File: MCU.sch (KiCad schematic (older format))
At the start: 13 parts, among them U5 STM32F405R, Y1 Crystal_8MHz_18pf

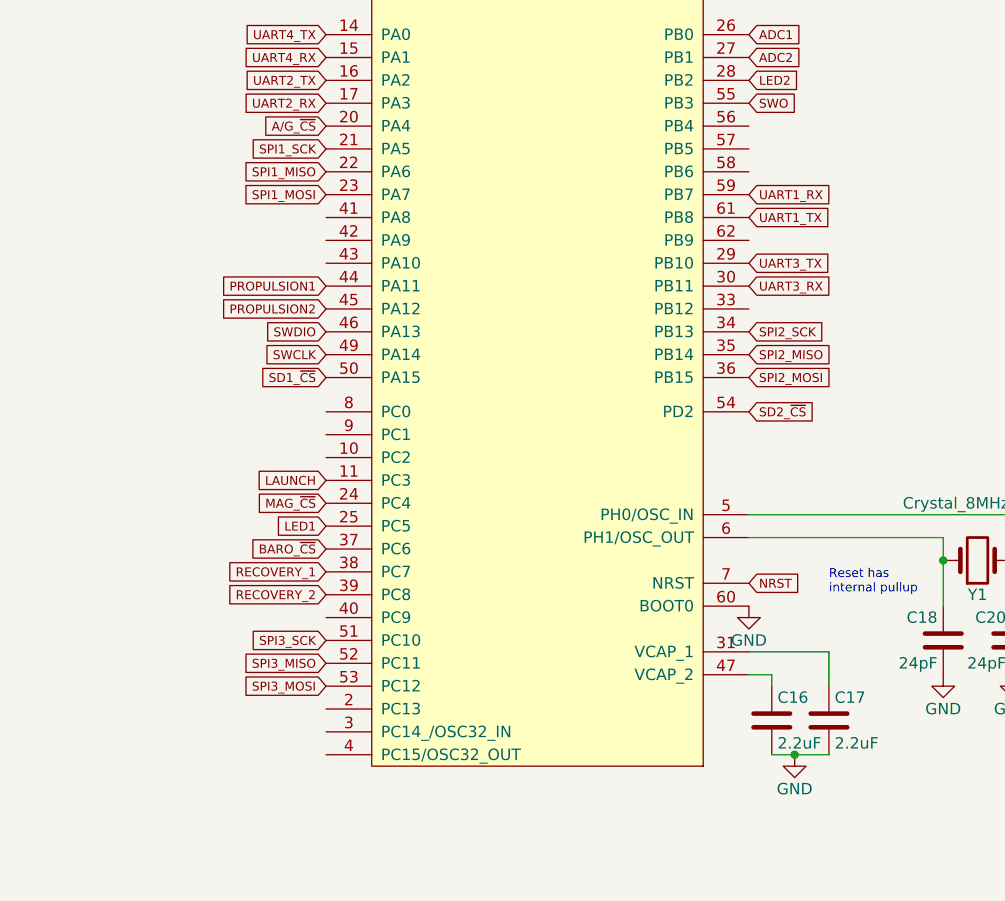
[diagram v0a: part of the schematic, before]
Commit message: Bring schematic in line with PCB. Previous update broke this.
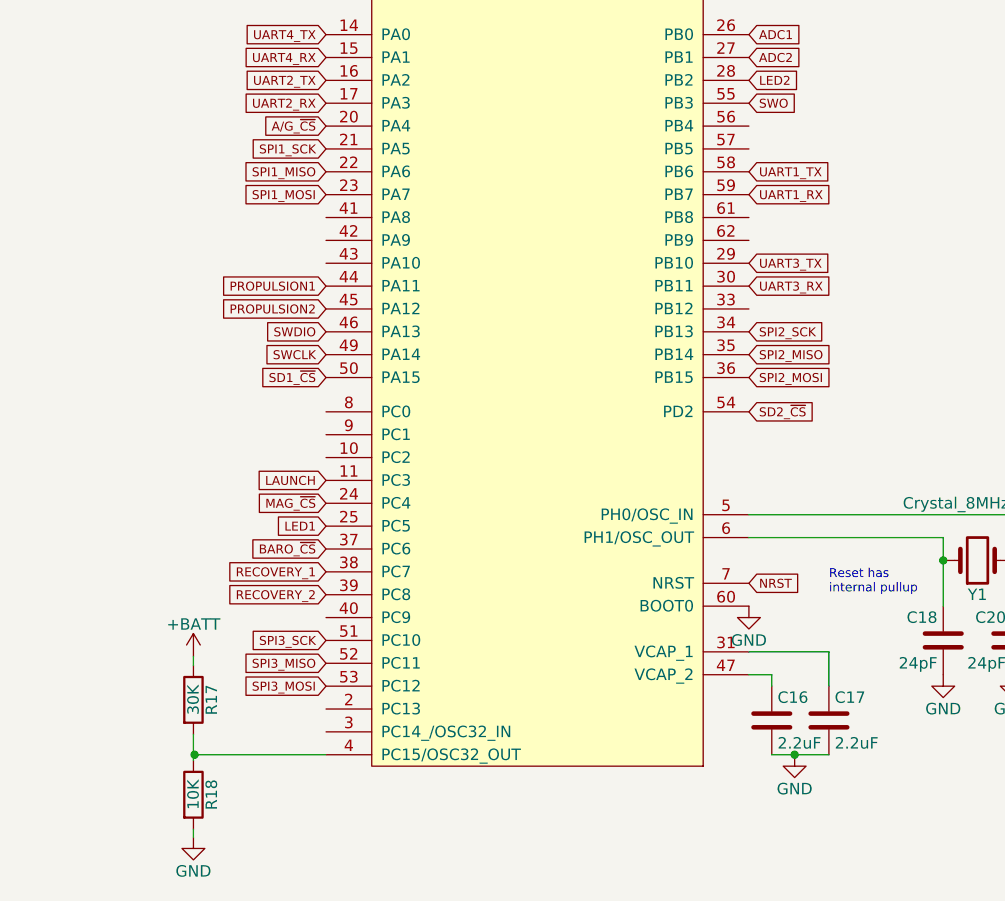
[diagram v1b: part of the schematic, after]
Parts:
- added R17: 30K, Resistors_SMD:R_0603, symbol R
- added R18: 10K, Resistors_SMD:R_0603, symbol R
- C16, C17, C18, C19, C20, C21, C22, C23, C24, C25, C26: footprint Capacitor_SMD:C_0603_1608Metric -> Capacitors_SMD:C_0603
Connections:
- net GND: now also R18.2
- net UART1_TX: now also U5.58 (PB6); no longer U5.61 (PB8)
- net at U5.4 (PC15/OSC32_OUT): now also R17.2, R18.1
- new net +BATT: R17.1
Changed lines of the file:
@@
 EESchema Schematic File Version 2
-LIBS:74xgxx
+LIBS:power
+LIBS:device
+LIBS:switches
+LIBS:relays
+LIBS:motors
+LIBS:transistors
+LIBS:conn
+LIBS:linear
+LIBS:regul
 LIBS:74xx
-LIBS:ac-dc
-LIBS:actel
+LIBS:cmos4000
 LIBS:adc-dac
-LIBS:allegro
-LIBS:Altera
-LIBS:analog_devices
+LIBS:memory
+LIBS:xilinx
+LIBS:microcontrollers
+LIBS:dsp
+LIBS:microchip
 LIBS:analog_switches
+LIBS:motorola
+LIBS:texas
+LIBS:intel
+LIBS:audio
+LIBS:interface
+LIBS:digital-audio
+LIBS:philips
+LIBS:display
+LIBS:cypress
+LIBS:siliconi
+LIBS:opto
 LIBS:atmel
-LIBS:audio
-LIBS:battery_management
-LIBS:bbd
-LIBS:bosch
-LIBS:brooktre
-LIBS:cmos_ieee
-LIBS:cmos4000
-LIBS:conn
 LIBS:contrib
-LIBS:cypress
-LIBS:dc-dc
-LIBS:device
-LIBS:digital-audio
-LIBS:diode
-LIBS:display
-LIBS:dsp
-LIBS:elec-unifil
-LIBS:ESD_Protection
-LIBS:ftdi
-LIBS:gennum
-LIBS:graphic_symbols
-LIBS:hc11
-LIBS:infineon
-LIBS:intel
-LIBS:interface
-LIBS:intersil
-LIBS:ir
-LIBS:Lattice
-LIBS:leds
-LIBS:LEM
-LIBS:linear
-LIBS:logic_programmable
-LIBS:maxim
+LIBS:valves
 LIBS:mechanical
-LIBS:memory
-LIBS:microchip
-LIBS:microchip_dspic33dsc
-LIBS:microchip_pic10mcu
-LIBS:microchip_pic12mcu
-LIBS:microchip_pic16mcu
-LIBS:microchip_pic18mcu
-LIBS:microchip_pic24mcu
-LIBS:microchip_pic32mcu
-LIBS:microcontrollers
-LIBS:modules
-LIBS:motor_drivers
-LIBS:motorola
-LIBS:motors
-LIBS:msp430
-LIBS:nordicsemi
-LIBS:nxp
-LIBS:nxp_armmcu
-LIBS:onsemi
-LIBS:opto
-LIBS:Oscillators
-LIBS:philips
-LIBS:power
-LIBS:Power_Management
-LIBS:powerint
-LIBS:pspice
-LIBS:references
-LIBS:regul
-LIBS:relays
-LIBS:rfcom
-LIBS:RFSolutions
-LIBS:sensors
-LIBS:silabs
-LIBS:siliconi
-LIBS:stm8
-LIBS:stm32
-LIBS:supertex
-LIBS:switches
-LIBS:texas
-LIBS:transf
-LIBS:transistors
-LIBS:triac_thyristor
-LIBS:ttl_ieee
-LIBS:valves
-LIBS:video
-LIBS:wiznet
-LIBS:Worldsemi
-LIBS:Xicor
-LIBS:xilinx
-LIBS:zetex
-LIBS:Zilog
 LIBS:AndromedaV2-cache
 EELAYER 25 0
@@
 F 0 "C19" H 6450 1800 50  0000 L CNN
 F 1 "10uF" H 6450 1600 50  0000 L CNN
-F 2 "Capacitor_SMD:C_0603_1608Metric" H 6463 1550 50  0001 C CNN
+F 2 "Capacitors_SMD:C_0603" H 6463 1550 50  0001 C CNN
 F 3 "" H 6425 1700 50  0001 C CNN
 	1    6425 1700
@@
 F 0 "C21" H 6750 1800 50  0000 L CNN
 F 1 "0.1uF" H 6750 1600 50  0000 L CNN
-F 2 "Capacitor_SMD:C_0603_1608Metric" H 6763 1550 50  0001 C CNN
+F 2 "Capacitors_SMD:C_0603" H 6763 1550 50  0001 C CNN
 F 3 "" H 6725 1700 50  0001 C CNN
 	1    6725 1700
@@
 F 0 "C22" H 7050 1800 50  0000 L CNN
 F 1 "0.1uF" H 7050 1600 50  0000 L CNN
-F 2 "Capacitor_SMD:C_0603_1608Metric" H 7063 1550 50  0001 C CNN
+F 2 "Capacitors_SMD:C_0603" H 7063 1550 50  0001 C CNN
 F 3 "" H 7025 1700 50  0001 C CNN
 	1    7025 1700
@@
 F 0 "C24" H 7350 1800 50  0000 L CNN
 F 1 "0.1uF" H 7350 1600 50  0000 L CNN
-F 2 "Capacitor_SMD:C_0603_1608Metric" H 7363 1550 50  0001 C CNN
+F 2 "Capacitors_SMD:C_0603" H 7363 1550 50  0001 C CNN
 F 3 "" H 7325 1700 50  0001 C CNN
 	1    7325 1700
@@
 $EndComp
 $Comp
-L +3.3V #PWR30
+L +3.3V #PWR025
 U 1 1 59D0A72F
 P 6425 1450
-F 0 "#PWR30" H 6425 1300 50  0001 C CNN
+F 0 "#PWR025" H 6425 1300 50  0001 C CNN
 F 1 "+3.3V" H 6425 1590 50  0000 C CNN
 F 2 "" H 6425 1450 50  0001 C CNN
@@
 $EndComp
 $Comp
-L GND #PWR31
+L GND #PWR026
 U 1 1 59D0A735
 P 6425 1950
-F 0 "#PWR31" H 6425 1700 50  0001 C CNN
+F 0 "#PWR026" H 6425 1700 50  0001 C CNN
 F 1 "GND" H 6425 1800 50  0000 C CNN
 F 2 "" H 6425 1950 50  0001 C CNN
@@
 F 0 "C23" H 7300 2850 50  0000 L CNN
 F 1 "1uF" H 7300 2650 50  0000 L CNN
-F 2 "Capacitor_SMD:C_0603_1608Metric" H 7313 2600 50  0001 C CNN
+F 2 "Capacitors_SMD:C_0603" H 7313 2600 50  0001 C CNN
 F 3 "" H 7275 2750 50  0001 C CNN
 	1    7275 2750
@@
 F 0 "C25" H 7600 2850 50  0000 L CNN
 F 1 "10nF" H 7600 2650 50  0000 L CNN
-F 2 "Capacitor_SMD:C_0603_1608Metric" H 7613 2600 50  0001 C CNN
+F 2 "Capacitors_SMD:C_0603" H 7613 2600 50  0001 C CNN
 F 3 "" H 7575 2750 50  0001 C CNN
 	1    7575 2750
@@
 $EndComp
 $Comp
-L +3.3V #PWR33
+L +3.3V #PWR027
 U 1 1 59D0A749
 P 7275 2500
-F 0 "#PWR33" H 7275 2350 50  0001 C CNN
+F 0 "#PWR027" H 7275 2350 50  0001 C CNN
 F 1 "+3.3V" H 7275 2640 50  0000 C CNN
 F 2 "" H 7275 2500 50  0001 C CNN
@@
 $EndComp
 $Comp
-L GND #PWR34
+L GND #PWR028
 U 1 1 59D0A74F
 P 7275 3000
-F 0 "#PWR34" H 7275 2750 50  0001 C CNN
+F 0 "#PWR028" H 7275 2750 50  0001 C CNN
 F 1 "GND" H 7275 2850 50  0000 C CNN
 F 2 "" H 7275 3000 50  0001 C CNN
@@
 F 0 "C20" H 6725 6500 50  0000 L CNN
 F 1 "24pF" H 6725 6300 50  0000 L CNN
-F 2 "Capacitor_SMD:C_0603_1608Metric" H 6738 6250 50  0001 C CNN
+F 2 "Capacitors_SMD:C_0603" H 6738 6250 50  0001 C CNN
 F 3 "" H 6700 6400 50  0001 C CNN
 	1    6700 6400
@@
 F 0 "C18" H 6425 6500 50  0000 L CNN
 F 1 "24pF" H 6425 6300 50  0000 L CNN
-F 2 "Capacitor_SMD:C_0603_1608Metric" H 6438 6250 50  0001 C CNN
+F 2 "Capacitors_SMD:C_0603" H 6438 6250 50  0001 C CNN
 F 3 "" H 6400 6400 50  0001 C CNN
 	1    6400 6400
@@
 $EndComp
 $Comp
-L GND #PWR32
+L GND #PWR029
 U 1 1 59D0A76A
 P 6700 6550
-F 0 "#PWR32" H 6700 6300 50  0001 C CNN
+F 0 "#PWR029" H 6700 6300 50  0001 C CNN
 F 1 "GND" H 6700 6400 50  0000 C CNN
 F 2 "" H 6700 6550 50  0001 C CNN
@@
 $EndComp
 $Comp
-L GND #PWR29
+L GND #PWR030
 U 1 1 59D0A770
 P 6400 6550
-F 0 "#PWR29" H 6400 6300 50  0001 C CNN
+F 0 "#PWR030" H 6400 6300 50  0001 C CNN
 F 1 "GND" H 6400 6400 50  0000 C CNN
 F 2 "" H 6400 6550 50  0001 C CNN
@@
 Reset has \ninternal pullup
 $Comp
-L GND #PWR26
+L GND #PWR031
 U 1 1 59D0A777
 P 5550 6250
-F 0 "#PWR26" H 5550 6000 50  0001 C CNN
+F 0 "#PWR031" H 5550 6000 50  0001 C CNN
 F 1 "GND" H 5550 6100 50  0000 C CNN
 F 2 "" H 5550 6250 50  0001 C CNN
@@
 Text GLabel 3700 3850 0    39   Input ~ 0
 UART4_RX
-Text GLabel 5550 4550 2    39   Input ~ 0
+Text GLabel 5550 4350 2    39   Input ~ 0
 UART1_TX
 Text GLabel 5550 4450 2    39   Input ~ 0
@@
 SWO
 $Comp
-L +3.3V #PWR25
+L +3.3V #PWR032
 U 1 1 59EBE46E
 P 3700 1800
-F 0 "#PWR25" H 3700 1650 50  0001 C CNN
+F 0 "#PWR032" H 3700 1650 50  0001 C CNN
 F 1 "+3.3V" H 3700 1940 50  0000 C CNN
 F 2 "" H 3700 1800 50  0001 C CNN
@@
 $EndComp
 $Comp
-L GND #PWR27
+L GND #PWR033
 U 1 1 59EBE4CD
 P 5600 3175
-F 0 "#PWR27" H 5600 2925 50  0001 C CNN
+F 0 "#PWR033" H 5600 2925 50  0001 C CNN
 F 1 "GND" H 5600 3025 50  0000 C CNN
 F 2 "" H 5600 3175 50  0001 C CNN
@@
 F 0 "C26" H 7650 1800 50  0000 L CNN
 F 1 "0.1uF" H 7650 1600 50  0000 L CNN
-F 2 "Capacitor_SMD:C_0603_1608Metric" H 7663 1550 50  0001 C CNN
+F 2 "Capacitors_SMD:C_0603" H 7663 1550 50  0001 C CNN
 F 3 "" H 7625 1700 50  0001 C CNN
 	1    7625 1700
@@
 F 0 "C16" H 5675 6850 50  0000 L CNN
 F 1 "2.2uF" H 5675 6650 50  0000 L CNN
-F 2 "Capacitor_SMD:C_0603_1608Metric" H 5688 6600 50  0001 C CNN
+F 2 "Capacitors_SMD:C_0603" H 5688 6600 50  0001 C CNN
 F 3 "" H 5650 6750 50  0001 C CNN
 	1    5650 6750
@@
 F 0 "C17" H 5925 6850 50  0000 L CNN
 F 1 "2.2uF" H 5925 6650 50  0000 L CNN
-F 2 "Capacitor_SMD:C_0603_1608Metric" H 5938 6600 50  0001 C CNN
+F 2 "Capacitors_SMD:C_0603" H 5938 6600 50  0001 C CNN
 F 3 "" H 5900 6750 50  0001 C CNN
 	1    5900 6750
@@
 $EndComp
 $Comp
-L GND #PWR28
+L GND #PWR034
 U 1 1 59EC0B51
 P 5750 6900
-F 0 "#PWR28" H 5750 6650 50  0001 C CNN
+F 0 "#PWR034" H 5750 6650 50  0001 C CNN
 F 1 "GND" H 5750 6750 50  0000 C CNN
 F 2 "" H 5750 6900 50  0001 C CNN
@@
 Text GLabel 5550 4850 2    39   Input ~ 0
 UART3_RX
+$Comp
+L R R18
+U 1 1 5AF18545
+P 3120 7075
+F 0 "R18" V 3200 7075 50  0000 C CNN
+F 1 "10K" V 3120 7075 50  0000 C CNN
+F 2 "Resistors_SMD:R_0603" V 3050 7075 50  0001 C CNN
+F 3 "" H 3120 7075 50  0001 C CNN
+	1    3120 7075
+	1    0    0    -1
+$EndComp
+$Comp
+L R R17
+U 1 1 5AF18698
+P 3120 6660
+F 0 "R17" V 3200 6660 50  0000 C CNN
+F 1 "30K" V 3120 6660 50  0000 C CNN
+F 2 "Resistors_SMD:R_0603" V 3050 6660 50  0001 C CNN
+F 3 "" H 3120 6660 50  0001 C CNN
+	1    3120 6660
+	1    0    0    -1
+$EndComp
+Wire Wire Line
+	3700 6900 3120 6900
+Wire Wire Line
+	3120 6900 3120 6925
+Wire Wire Line
+	3120 6810 3120 6895
+Wire Wire Line
+	3120 6895 3125 6895
+Wire Wire Line
+	3125 6895 3125 6900
+Connection ~ 3125 6900
+$Comp
+L +BATT #PWR035
+U 1 1 5AF18909
+P 3120 6470
+F 0 "#PWR035" H 3120 6320 50  0001 C CNN
+F 1 "+BATT" H 3120 6610 50  0000 C CNN
+F 2 "" H 3120 6470 50  0001 C CNN
+F 3 "" H 3120 6470 50  0001 C CNN
+	1    3120 6470
+	1    0    0    -1
+$EndComp
+Wire Wire Line
+	3120 6470 3120 6510
+$Comp
+L GND #PWR036
+U 1 1 5AF18BA0
+P 3120 7260
+F 0 "#PWR036" H 3120 7010 50  0001 C CNN
+F 1 "GND" H 3120 7110 50  0000 C CNN
+F 2 "" H 3120 7260 50  0001 C CNN
+F 3 "" H 3120 7260 50  0001 C CNN
+	1    3120 7260
+	1    0    0    -1
+$EndComp
+Wire Wire Line
+	3120 7225 3120 7260
 $EndSCHEMATC

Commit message: Final design published. Gerbers and PDF schematic generated
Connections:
- net Fan_ctrl: now reaches U5.57 (PB5)
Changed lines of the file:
@@
 $EndComp
 $Comp
-L +3.3V #PWR024
+L +3.3V #PWR026
 U 1 1 59D0A72F
 P 6425 1450
-F 0 "#PWR024" H 6425 1300 50  0001 C CNN
+F 0 "#PWR026" H 6425 1300 50  0001 C CNN
 F 1 "+3.3V" H 6425 1590 50  0000 C CNN
 F 2 "" H 6425 1450 50  0001 C CNN
@@
 $EndComp
 $Comp
-L GND #PWR025
+L GND #PWR027
 U 1 1 59D0A735
 P 6425 1950
-F 0 "#PWR025" H 6425 1700 50  0001 C CNN
+F 0 "#PWR027" H 6425 1700 50  0001 C CNN
 F 1 "GND" H 6425 1800 50  0000 C CNN
 F 2 "" H 6425 1950 50  0001 C CNN
@@
 $EndComp
 $Comp
-L +3.3V #PWR026
+L +3.3V #PWR028
 U 1 1 59D0A749
 P 7275 2500
-F 0 "#PWR026" H 7275 2350 50  0001 C CNN
+F 0 "#PWR028" H 7275 2350 50  0001 C CNN
 F 1 "+3.3V" H 7275 2640 50  0000 C CNN
 F 2 "" H 7275 2500 50  0001 C CNN
@@
 $EndComp
 $Comp
-L GND #PWR027
+L GND #PWR029
 U 1 1 59D0A74F
 P 7275 3000
-F 0 "#PWR027" H 7275 2750 50  0001 C CNN
+F 0 "#PWR029" H 7275 2750 50  0001 C CNN
 F 1 "GND" H 7275 2850 50  0000 C CNN
 F 2 "" H 7275 3000 50  0001 C CNN
@@
 $EndComp
 $Comp
-L GND #PWR028
+L GND #PWR030
 U 1 1 59D0A76A
 P 6700 6550
-F 0 "#PWR028" H 6700 6300 50  0001 C CNN
+F 0 "#PWR030" H 6700 6300 50  0001 C CNN
 F 1 "GND" H 6700 6400 50  0000 C CNN
 F 2 "" H 6700 6550 50  0001 C CNN
@@
 $EndComp
 $Comp
-L GND #PWR029
+L GND #PWR031
 U 1 1 59D0A770
 P 6400 6550
-F 0 "#PWR029" H 6400 6300 50  0001 C CNN
+F 0 "#PWR031" H 6400 6300 50  0001 C CNN
 F 1 "GND" H 6400 6400 50  0000 C CNN
 F 2 "" H 6400 6550 50  0001 C CNN
@@
 Reset has \ninternal pullup
 $Comp
-L GND #PWR030
+L GND #PWR032
 U 1 1 59D0A777
 P 5550 6250
-F 0 "#PWR030" H 5550 6000 50  0001 C CNN
+F 0 "#PWR032" H 5550 6000 50  0001 C CNN
 F 1 "GND" H 5550 6100 50  0000 C CNN
 F 2 "" H 5550 6250 50  0001 C CNN
@@
 SWO
 $Comp
-L +3.3V #PWR031
+L +3.3V #PWR033
 U 1 1 59EBE46E
 P 3700 1800
-F 0 "#PWR031" H 3700 1650 50  0001 C CNN
+F 0 "#PWR033" H 3700 1650 50  0001 C CNN
 F 1 "+3.3V" H 3700 1940 50  0000 C CNN
 F 2 "" H 3700 1800 50  0001 C CNN
@@
 $EndComp
 $Comp
-L GND #PWR032
+L GND #PWR034
 U 1 1 59EBE4CD
 P 5600 3175
-F 0 "#PWR032" H 5600 2925 50  0001 C CNN
+F 0 "#PWR034" H 5600 2925 50  0001 C CNN
 F 1 "GND" H 5600 3025 50  0000 C CNN
 F 2 "" H 5600 3175 50  0001 C CNN
@@
 $EndComp
 $Comp
-L GND #PWR033
+L GND #PWR035
 U 1 1 59EC0B51
 P 5750 6900
-F 0 "#PWR033" H 5750 6650 50  0001 C CNN
+F 0 "#PWR035" H 5750 6650 50  0001 C CNN
 F 1 "GND" H 5750 6750 50  0000 C CNN
 F 2 "" H 5750 6900 50  0001 C CNN
@@
 Connection ~ 3125 6900
 $Comp
-L +BATT #PWR034
+L +BATT #PWR036
 U 1 1 5AF18909
 P 3120 6470
-F 0 "#PWR034" H 3120 6320 50  0001 C CNN
+F 0 "#PWR036" H 3120 6320 50  0001 C CNN
 F 1 "+BATT" H 3120 6610 50  0000 C CNN
 F 2 "" H 3120 6470 50  0001 C CNN
@@
 	3120 6470 3120 6510
 $Comp
-L GND #PWR035
+L GND #PWR037
 U 1 1 5AF18BA0
 P 3120 7260
-F 0 "#PWR035" H 3120 7010 50  0001 C CNN
+F 0 "#PWR037" H 3120 7010 50  0001 C CNN
 F 1 "GND" H 3120 7110 50  0000 C CNN
 F 2 "" H 3120 7260 50  0001 C CNN
@@
 Wire Wire Line
 	3120 7225 3120 7260
+Text GLabel 5550 4250 2    39   Input ~ 0
+Fan_ctrl
 $EndSCHEMATC
